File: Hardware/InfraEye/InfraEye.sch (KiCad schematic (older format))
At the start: 11 parts, among them Q1 Q_NPN_BCE, U1 MLX90640, U2 ESP32-WROOM-32, U3 TFT_SPI_24_LCD, U4 MLX90640

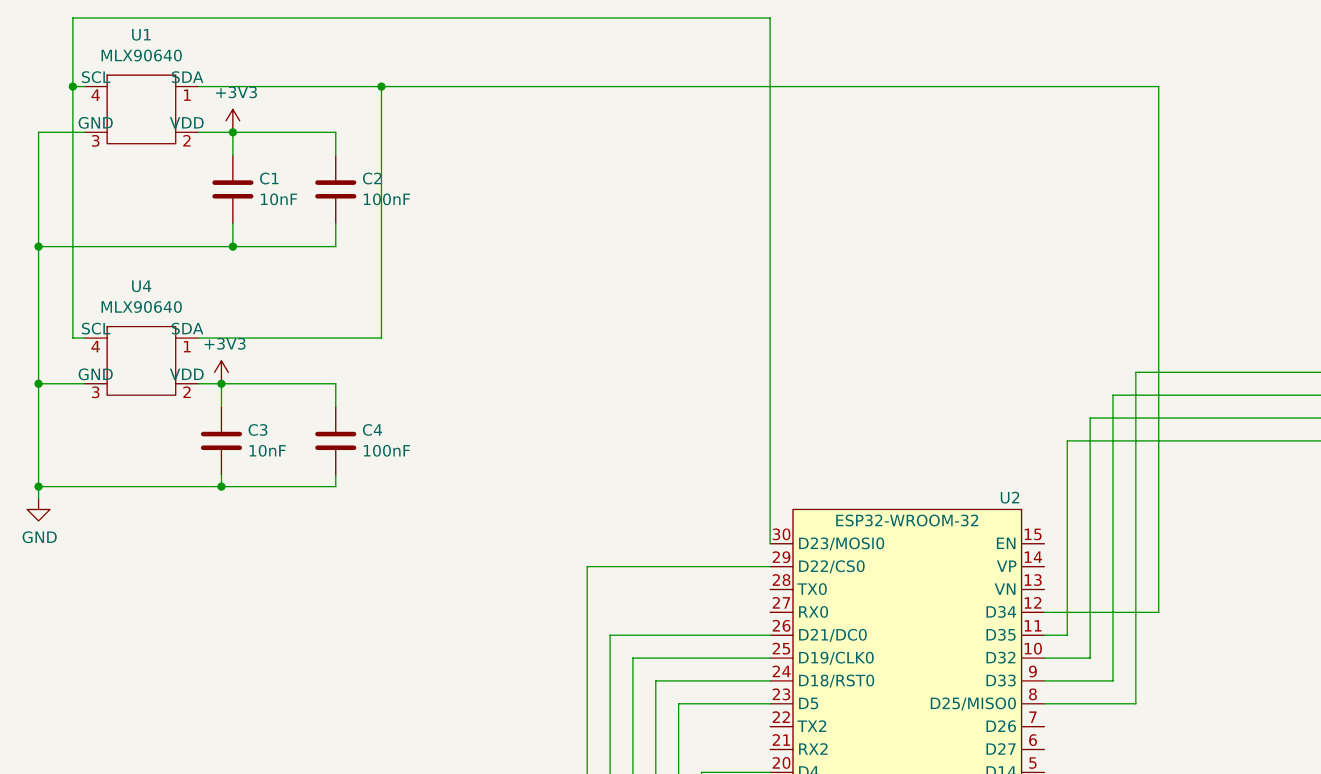
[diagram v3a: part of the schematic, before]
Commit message: Swapped I2C lines for better trace routing Further improvemets to board, added holes for easier board separation.
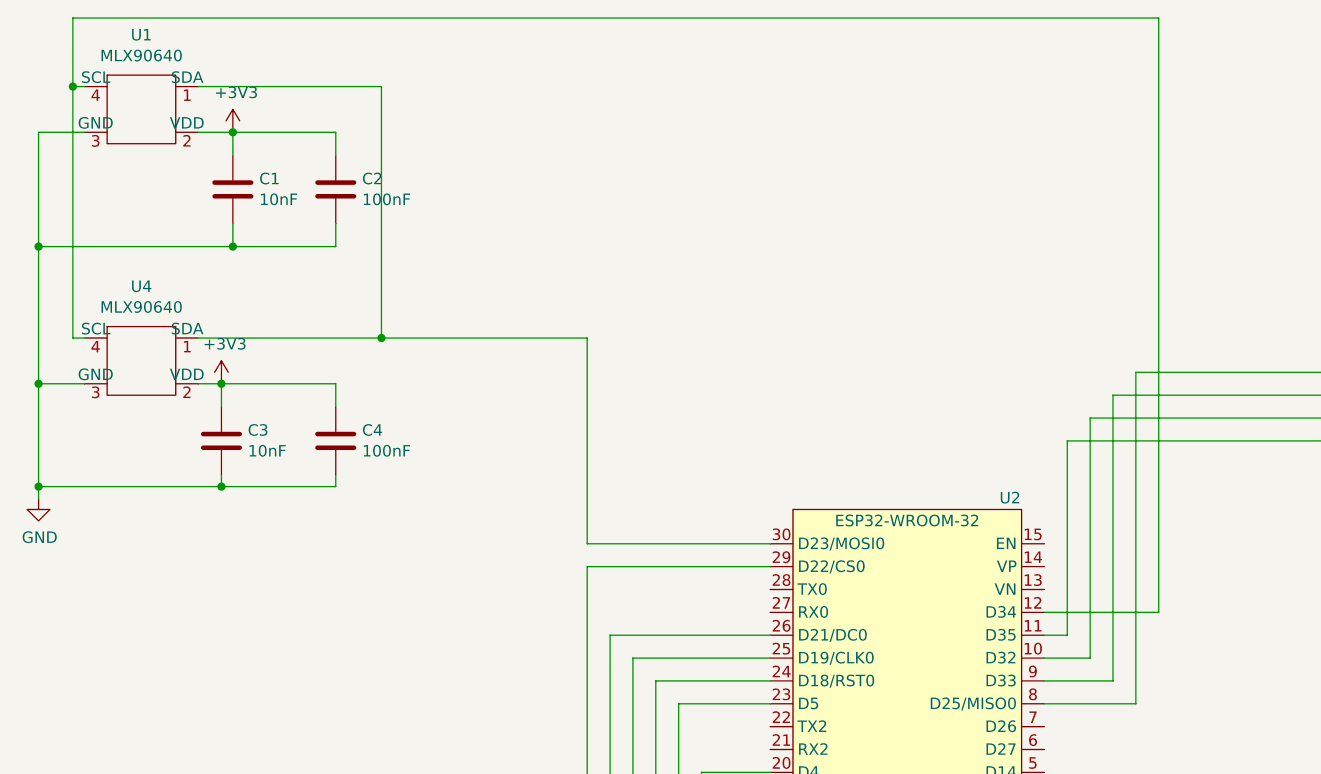
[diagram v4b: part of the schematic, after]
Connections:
- net at U1.1 (SDA), U4.1 (SDA): now also U2.30 (D23/MOSI0); no longer U2.12 (D34)
- net at U1.4 (SCL), U4.4 (SCL): now also U2.12 (D34); no longer U2.30 (D23/MOSI0)
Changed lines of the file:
@@
 $EndComp
-Wire Wire Line
-	1700 2200 2500 2200
 Wire Wire Line
 	1200 2200 1150 2200
@@
 	1    0    0    -1
 $EndComp
-Connection ~ 2500 1100
 $Comp
 L power:+3V3 #PWR0104
@@
 	5900 3400 5400 3400
 Wire Wire Line
-	1150 800  4200 800
-Wire Wire Line
-	5900 3400 5900 1100
-Wire Wire Line
-	2500 1100 5900 1100
-Wire Wire Line
-	4200 3100 4200 800
-Wire Wire Line
 	3400 3200 3400 5400
 Wire Wire Line
@@
 Wire Wire Line
 	3500 5900 4450 5900
+Wire Wire Line
+	5900 800  5900 3400
+Wire Wire Line
+	1150 800  5900 800
+Wire Wire Line
+	4200 3100 3400 3100
+Wire Wire Line
+	3400 3100 3400 2200
+Wire Wire Line
+	1700 2200 2500 2200
+Connection ~ 2500 2200
+Wire Wire Line
+	2500 2200 3400 2200
 $EndSCHEMATC

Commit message: Added AC power supply
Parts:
- added C? (x2): CP, symbol Device:CP
- added D? (x4): D, symbol Device:D
- added D?: D_Zener, symbol Device:D_Zener
- added J?: Conn_01x03_Male, symbol Connector:Conn_01x03_Male
- added U?: LT1129-3.3_SOT223, Package_TO_SOT_SMD:SOT-223-3_TabPin2, symbol Regulator_Linear:LT1129-3.3_SOT223
- U2: symbol InfraEye:ESP32-WROOM-32 -> InfraEye-rescue:ESP32-WROOM-32-InfraEye
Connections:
- net labels added: +5V
- wire segments 118 -> 145
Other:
- note added: "Component placement legend:\nB - Basic components - always populated\nW - WIFI version\nL - LCD version\nA - AC power supply\nR - Relay\nO - LCD backlight always on"

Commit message: AC power supply added also to PCB
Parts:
- added R3: R, Resistor_SMD:R_1206_3216Metric, symbol Device:R
- C5, C6: renamed from C?; footprint (none) -> Capacitor_THT:C_Radial_D5.0mm_H11.0mm_P2.00mm
- D1, D2, D3, D4, D5: renamed from D?; footprint (none) -> Diode_SMD:D_1206_3216Metric
- J1: renamed from J?; footprint (none) -> Connector:FanPinHeader_1x03_P2.54mm_Vertical
- gave numbers to parts that had none: 1
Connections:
- wire segments 145 -> 149
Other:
- note added: "Power supply"
